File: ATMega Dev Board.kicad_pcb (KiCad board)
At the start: 4 copper layers, 84 x 38.1 mm, 50 parts, among them J1 Conn_01x13, J2 Conn_01x09, J4 SPI header, J5 USB-C_31-M-12, Q1 S8050, Q2 2N7002, Q3 HL6042, Q4 HL6042, SW1 SW_SPST, SW2 SW_SPST, U1 ATmega32A-A, U2 CH340C, U3 USBLC6-2P6, X1 16MHz

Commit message: Rev B layout
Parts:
- removed the G*** at (70.3, 71.7)
- added FID1: Fiducial, Fiducial:Fiducial_1mm_Mask2mm, F.Cu at (47.6, 48.4)
- added FID2: Fiducial, Fiducial:Fiducial_1mm_Mask2mm, F.Cu at (47.6, 82.4)
- added FID3: Fiducial, Fiducial:Fiducial_1mm_Mask2mm, F.Cu at (116.6, 48.4)
- added G***: LOGO, ATMDBL:qrcode, F.Cu at (115.6, 78.4)
- added JP1: Jumper_2_Small_Open, Jumper:SolderJumper-2_P1.3mm_Open_Pad1.0x1.5mm, F.Cu at (92.9, 71.9)
- added JP2: Jumper_2_Small_Open, Jumper:SolderJumper-2_P1.3mm_Open_Pad1.0x1.5mm, F.Cu at (92.9, 75.9)
- added R5: 5k1, Capacitor_SMD:C_0603_1608Metric, F.Cu at (96.6, 71.9)
- added R6: 5k1, Resistor_SMD:R_0603_1608Metric, F.Cu at (96.6, 75.9)
- added R7: 4k7, Resistor_SMD:R_0603_1608Metric, F.Cu at (109.6, 68.9)
- H1, H2, H3, H4: footprint MountingHole:MountingHole_2.1mm -> MountingHole:MountingHole_3.2mm_M3_Pad_Via
- J4: renamed from J5; footprint FTBLib:USB_C_Receptacle_HRO_TYPE-C-31-M-12 -> ATMDBL:USB_C_Receptacle_HRO_TYPE-C-31-M-12
- LS1: footprint FTBLib:Buzzer_MLT-9650 -> ATMDBL:Buzzer_MLT-9650
- REF**: moved to F.Cu
- SW1, SW2: footprint FTBLib:Switch_TS-1088-AR02016 -> ATMDBL:Switch_TS-1088-AR02016
- U2: footprint Package_SO:SOIC-16_3.9x9.9mm_P1.27mm -> Package_SO:MSOP-10_3x3mm_P0.5mm
- moved R2 26.6 mm to (103.2, 57.6)
- moved D2 26.6 mm to (101.5, 57.9)
- moved D1 26.5 mm to (99.5, 57.9)
- moved R1 26.5 mm to (98.0, 57.6)
- moved SW1 24.6 mm to (97.5, 63.4)
- moved SW2 24.6 mm to (103.6, 63.4)
- moved D3 20.9 mm to (58.6, 58.5), turned to 0 degrees
- moved LS1 20.5 mm to (61.1, 65.4), turned to 0 degrees
- moved Q1 18.4 mm to (58.2, 73.0), turned to 0 degrees
- moved C13 17.4 mm to (114.6, 68.9)
- moved REF** 16.3 mm to (106.1, 78.4), turned to 0 degrees
- moved C14 15.6 mm to (120.3, 56.9), turned to 180 degrees
- moved R4 14.5 mm to (61.1, 73.0), turned to 90 degrees
- moved R9 14.0 mm to (107.5, 46.8)
- moved R8 13.9 mm to (103.5, 46.8)
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- renumbered C2 to C1, C7 to C10, C12 to C11, C13 to C12, C14 to C13, C6 to C14, C1 to C2, C9 to C5, C8 to C6, C5 to C7, C10 to C8, C11 to C9, D5 to D4, D4 to D5, J4 to J3, R2 to R1, R5 to R10, R6 to R11, R11 to R12, R3 to R2, R1 to R3
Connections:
- net /PC0 renamed /SCL
- net /PC1 renamed /SDA
- C11 pad 2: Net-(U2-~{DTR}) -> /DTR
- C13 pad 2: Net-(U2-V3) -> /V3
- C14 pad 1: VBUS -> VUSB
- R12 pad 1: VUSB -> VBUS
- U1 pad 25: /SW1 -> /SW2
- U1 pad 26: /SW2 -> /SW1
- U2 pad 1: GND -> /UD+
- U2 pad 10: unconnected-(U2-~{DSR}-Pad10) -> /V3
- U2 pad 2: /UTXD -> /UD-
- U2 pad 3: /URXD -> GND
- U2 pad 4: Net-(U2-V3) -> unconnected-(U2-~{RTS}-Pad4)
- U2 pad 5: /UD+ -> unconnected-(U2-~{CTS}-Pad5)
- U2 pad 6: /UD- -> /DTR
- U2 pad 7: unconnected-(U2-NC-Pad7) -> VCC
- U2 pad 8: unconnected-(U2-NC-Pad8) -> /UTXD
- U2 pad 9: unconnected-(U2-~{CTS}-Pad9) -> /URXD
- U3 pad 1: /UD+ -> /UD-
- U3 pad 3: /UD- -> /UD+
- U3 pad 4: /UD_N -> /UD_P
- U3 pad 6: /UD_P -> /UD_N
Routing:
- net VCC: track 175.3 -> 0.00 mm
- net VSPI: track 57.1 -> 0.00 mm
- net GND: track 50.4 -> 0.00 mm, vias 32 -> 0
- net /RST: track 48.0 -> 0.00 mm, vias 2 -> 0
- net /MISO: track 40.8 -> 0.00 mm, vias 2 -> 0
- net /UTXD: track 39.5 -> 0.00 mm, vias 2 -> 0
- net /URXD: track 39.0 -> 0.00 mm, vias 2 -> 0
- net /SCK: track 38.6 -> 0.00 mm, vias 2 -> 0
- net /MOSI: track 35.2 -> 0.00 mm, vias 2 -> 0
- net /SW2: track 33.0 -> 0.00 mm
- net Net-(U2-~{DTR}): track 30.9 -> 0.00 mm, vias 2 -> 0
- net /PB4: track 24.6 -> 0.00 mm, vias 1 -> 0
- net VUSB: track 24.4 -> 0.00 mm
- net /SW1: track 23.9 -> 0.00 mm
- net VBUS: track 23.4 -> 0.00 mm
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- removed copper zone on F.Cu, net GND
- removed copper zone on In1.Cu, net GND
- removed copper zone on In2.Cu, net GND
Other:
- board size 84 x 38.1 mm -> 88 x 43 mm
- board text added: "ATMega32 Demo Board Rev B - March 2026"
- board text added: "SCL"
- board text added: "SDA"
- board text removed: "5V ONLY!"
- board text removed: "ATMega32 Demo Board Rev A - March 2026 https://github.com/spassigl/ATMega32A-demo-board.git"

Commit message: tweaked layout
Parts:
- removed C14: 0.1u, Capacitor_SMD:C_0603_1608Metric
- removed the C3 at (73.1, 64.9)
- removed the C4 at (82.1, 74.4)
- removed the C5 at (83.1, 56.4)
- removed REF**: KiCad-Logo2_5mm_SilkScreen, Symbol:KiCad-Logo2_5mm_SilkScreen
- added C11: 10u, Capacitor_SMD:C_0805_2012Metric, F.Cu at (110.4, 48.1)
- added C12: 0.1u, Capacitor_SMD:C_0603_1608Metric, F.Cu at (103.6, 48.1)
- added G***: LOGO, ATMDBL:github, F.Cu at (108.6, 78.4)
- added R13: 0R, Resistor_SMD:R_0603_1608Metric, F.Cu at (106.9, 48.1)
- R11: footprint Capacitor_SMD:C_0603_1608Metric -> Resistor_SMD:R_0603_1608Metric
- U2: value CH340C -> CH340X
- moved FID3 29.4 mm to (121.6, 77.4)
- moved R5 16.8 mm to (80.6, 76.9), turned to 0 degrees
- moved G*** 13.5 mm to (102.1, 78.4)
- moved JP1 10.1 mm to (84.1, 76.9), turned to 180 degrees
- moved R1 10.0 mm to (95.7, 67.4), turned to 90 degrees
- moved R2 9.85 mm to (104.7, 67.4), turned to 90 degrees
- moved D1 9.80 mm to (97.2, 67.4)
- moved D2 9.63 mm to (103.2, 67.4)
- moved R8 7.34 mm to (106.1, 53.7)
- moved FID1 7.07 mm to (42.6, 53.4)
- moved FID2 7.07 mm to (42.6, 77.4)
- moved R9 6.49 mm to (113.9, 48.1)
- moved C1 4.00 mm to (74.1, 70.9), turned to -90 degrees
- moved R3 3.64 mm to (75.6, 59.4), turned to 0 degrees
- moved R7 3.51 mm to (109.3, 65.4)
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- renumbered C13 to C10, C6 to C3, C7 to C4, C8 to C5, C9 to C6, C10 to C7, C11 to C8, C12 to C9
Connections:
- D4 pad 5: VCC -> VSPI
- Q3 pad 2: VCC -> Net-(Q3-S)
- Q4 pad 2: VCC -> Net-(Q3-S)
- R9 pad 1: VCC -> Net-(Q3-S)
- U1 pad 23: /LED1 -> /LED2
- U1 pad 24: /LED2 -> /LED1
- U3 pad 1: /UD- -> /UD+
- U3 pad 3: /UD+ -> /UD-
- U3 pad 4: /UD_P -> /UD_N
- U3 pad 6: /UD_N -> /UD_P
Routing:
- net VCC: track 0.00 -> 177.7 mm, vias 0 -> 6
- net VSPI: track 0.00 -> 91.9 mm, vias 0 -> 2
- net /RST: track 0.00 -> 54.8 mm, vias 0 -> 2
- net /DTR: track 0.00 -> 45.4 mm, vias 0 -> 2
- net /URXD: track 0.00 -> 40.3 mm
- net /UTXD: track 0.00 -> 39.4 mm
- net /SCK: track 0.00 -> 38.6 mm
- net /MISO: track 0.00 -> 38.5 mm
- net GND: track 0.00 -> 37.3 mm, vias 0 -> 44
- net /MOSI: track 0.00 -> 36.0 mm, vias 0 -> 2
- net VUSB: track 0.00 -> 28.6 mm
- net VBUS: track 0.00 -> 26.8 mm
- net /SW2: track 0.00 -> 25.5 mm, vias 0 -> 2
- net /SPKR: track 0.00 -> 21.5 mm
- net /PA7: track 0.00 -> 21.1 mm, vias 0 -> 1
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- added copper zone on F.Cu, net GND
- added copper zone on In1.Cu, net GND
- added copper zone on In2.Cu, net GND
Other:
- outline, holes or cut-outs redrawn
- board text added: "ATMega32 Demo Board Rev B - 2026/03"
- board text removed: "ATMega32 Demo Board Rev B - March 2026"
- board text removed: "JLCJLCJLCJLC"

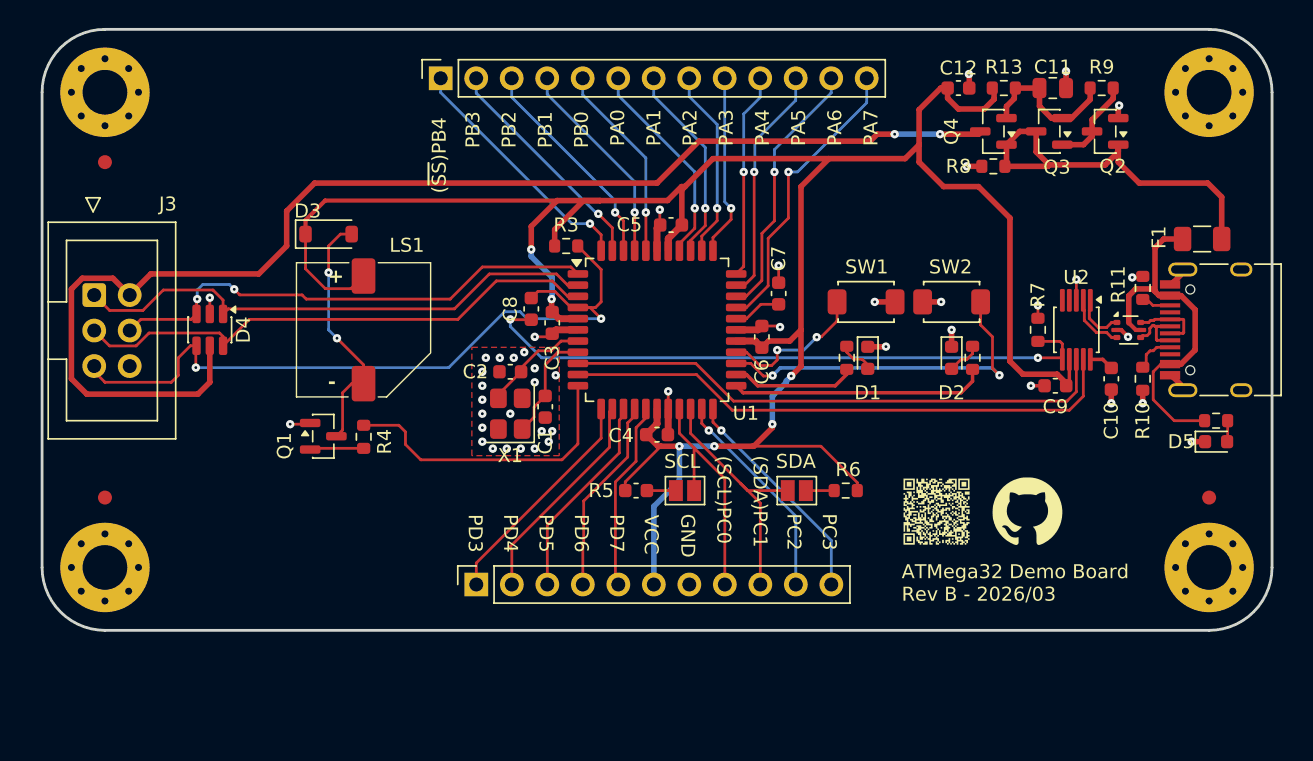
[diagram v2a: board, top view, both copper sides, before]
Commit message: added ADC/AREF components
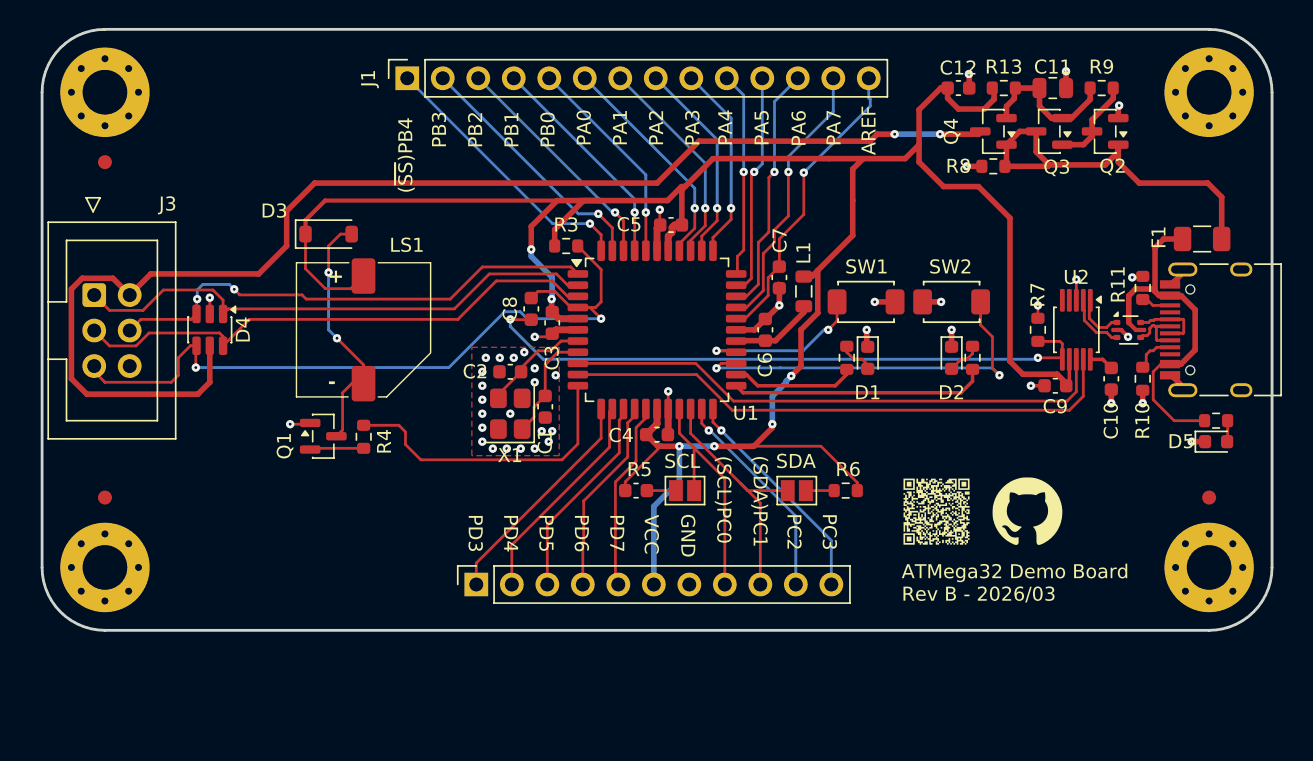
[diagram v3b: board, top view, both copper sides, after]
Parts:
- added L1: 10uH, Inductor_SMD:L_0805_2012Metric, F.Cu at (92.6, 62.6)
- J1: footprint Connector_PinSocket_2.54mm:PinSocket_1x13_P2.54mm_Vertical -> Connector_PinSocket_2.54mm:PinSocket_1x14_P2.54mm_Vertical
- moved J1 2.39 mm to (64.2, 47.4)
- moved C7 1.15 mm to (90.8, 61.6), turned to 90 degrees
- moved C6 0.56 mm to (89.8, 65.4)
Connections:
- C6 pad 1: VCC -> /AVCC
- C7 pad 2: Net-(U1-AREF) -> /AREF
- U1 pad 27: VCC -> /AVCC
- U1 pad 29: Net-(U1-AREF) -> /AREF
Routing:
- net /AREF: track 0.00 -> 21.6 mm, vias 0 -> 1
- net /AVCC: track 0.00 -> 6.12 mm
- net Net-(U1-AREF): track 3.26 -> 0.00 mm
- net VCC: track 177.7 -> 174.8 mm
- net /SW2: track 25.5 -> 27.8 mm
- net /PB4: track 17.9 -> 19.6 mm
- net /PB3: track 16.4 -> 18.2 mm
- net /SW1: track 10.7 -> 12.3 mm
- net /PA7: track 21.1 -> 19.7 mm
- net /PB2: track 15.7 -> 16.8 mm
- net /PA1: track 14.3 -> 15.3 mm
- net /PB0: track 14.2 -> 15.2 mm
- net /PA3: track 13.1 -> 14.1 mm
- net /PA5: track 16.9 -> 15.9 mm
- net /PB1: track 14.9 -> 15.9 mm
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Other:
- board text added: "0"
- board text added: "0 mm"
- board text added: "0.01 mm"
- board text added: "0.02"
- board text added: "0.03 mm"
- board text added: "0.035 mm"
- board text added: "0.1500 mm / 0.1500 mm"
- board text added: "0.2000 mm"
- board text added: "0.203 mm"
- board text added: "1"
- board text added: "1.03 mm"
- board text added: "1.5860 mm"
- board text added: "3.3"
- board text added: "4"
- board text added: "4.4"
- board text added: "4.6"
- board text added: "88.0000 mm x 43.0000 mm"
- board text added: "AREF"
- board text added: "B.Cu"
- board text added: "B.Mask"
- board text added: "B.Paste"
- board text added: "B.Silkscreen"
- board text added: "BOARD CHARACTERISTICS"
- board text added: "Board Thickness:"
- board text added: "Board overall dimensions:"
- board text added: "Bottom Silk Screen"
- board text added: "Bottom Solder Mask"
- board text added: "Bottom Solder Paste"
- board text added: "Castellated pads:"
- board text added: "Color"
- board text added: "Copper Finish:"
- board text added: "Copper Layer Count:"
- board text added: "Dielectric"
- board text added: "Edge card connectors:"
- board text added: "Epsilon R"
- board text added: "F.Cu"
- board text added: "F.Mask"
- board text added: "F.Paste"
- board text added: "F.Silkscreen"
- board text added: "FR4"
- board text added: "FR4 natural"
- board text added: "HAL lead-free"
- board text added: "Impedance Control:"
- board text added: "In1.Cu"
- board text added: "In2.Cu"
- board text added: "Layer Name"
- board text added: "Loss Tangent"
- board text added: "Material"
- board text added: "Min hole diameter:"
- board text added: "Min track/spacing:"
- board text added: "No"
- board text added: "Not specified"
- board text added: "Plated Board Edge:"
- board text added: "Thickness (mm)"
- board text added: "Top Silk Screen"
- board text added: "Top Solder Mask"
- board text added: "Top Solder Paste"
- board text added: "Type"
- board text added: "Yes"
- board text added: "copper"
- board text added: "core"
- board text added: "prepreg"

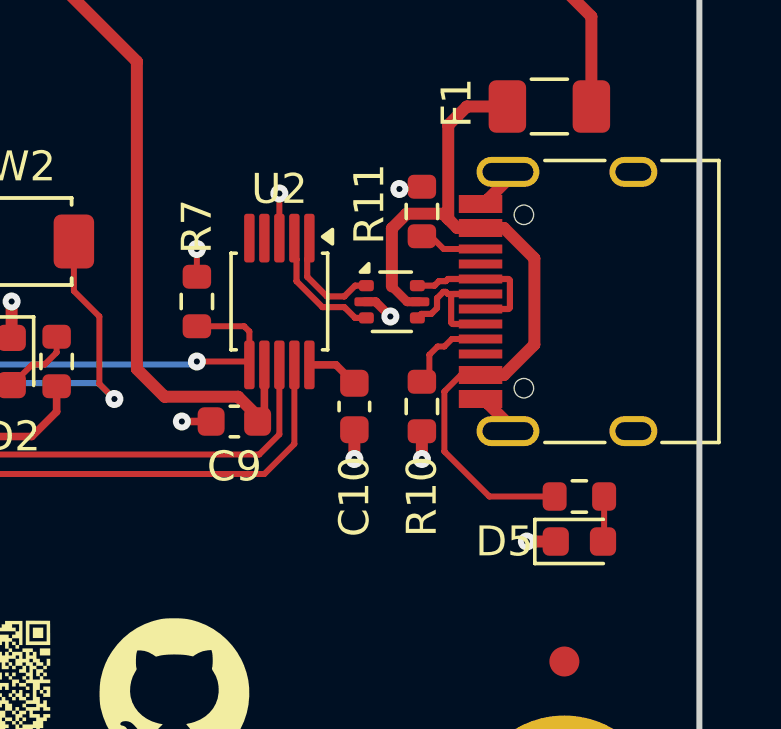
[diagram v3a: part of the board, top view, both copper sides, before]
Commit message: upgraded USB-C routing
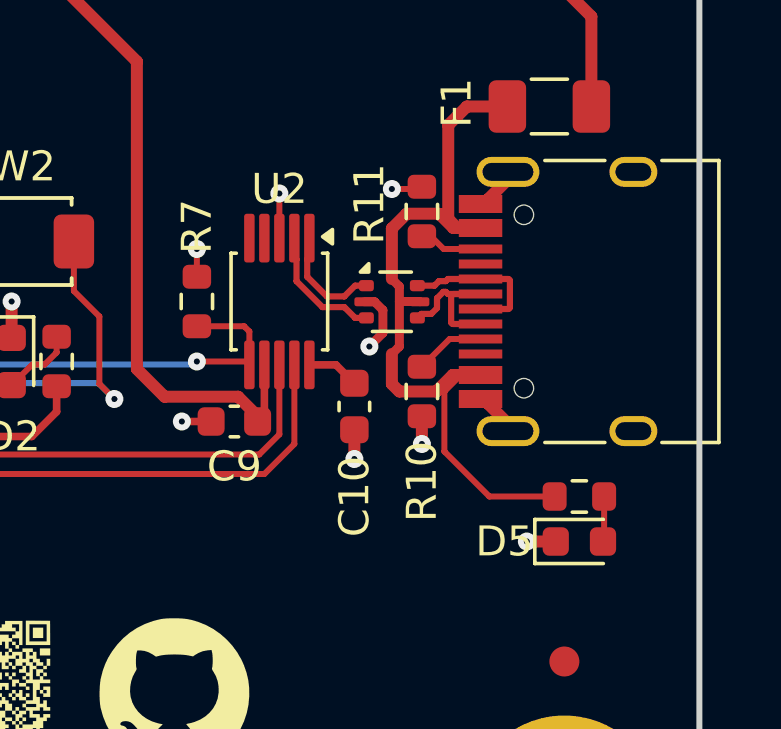
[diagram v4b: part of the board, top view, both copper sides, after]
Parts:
- moved R10 0.50 mm to (116.8, 68.4)
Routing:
- net GND: track 38.0 -> 39.3 mm
- net Net-(J4-CC1): track 3.07 -> 2.34 mm
